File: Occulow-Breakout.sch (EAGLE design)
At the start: 18 parts

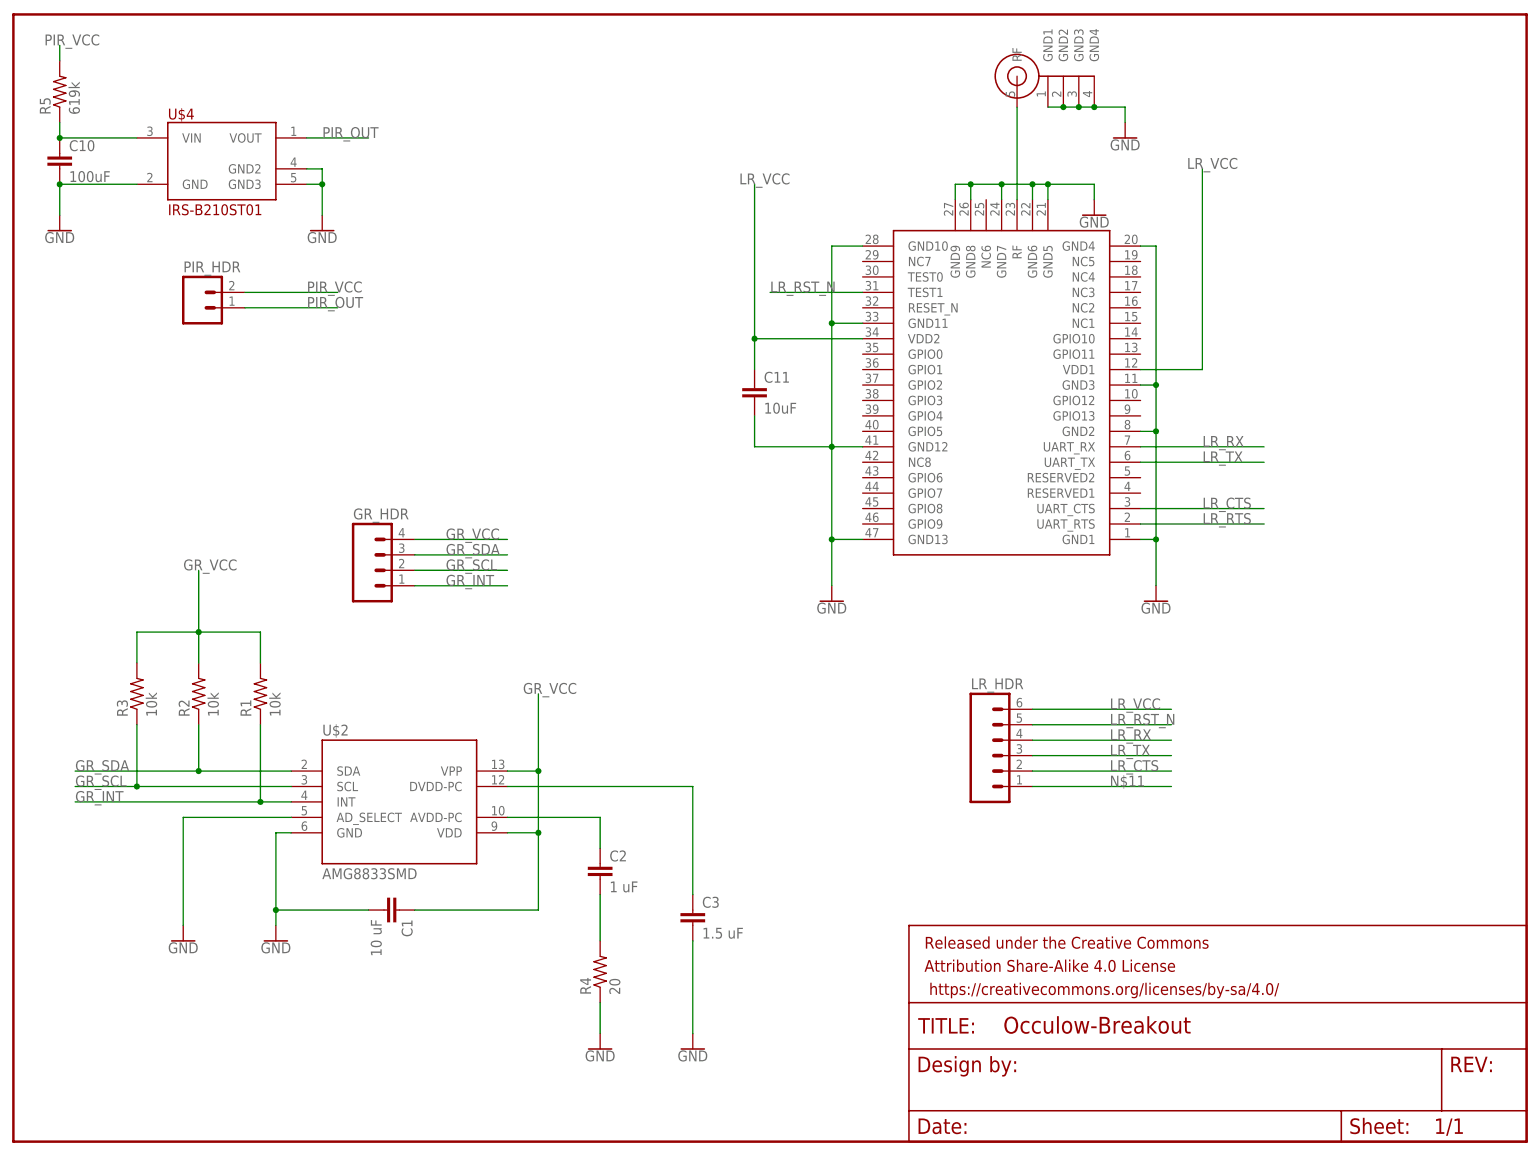
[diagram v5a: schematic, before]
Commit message: Ground pins on headers
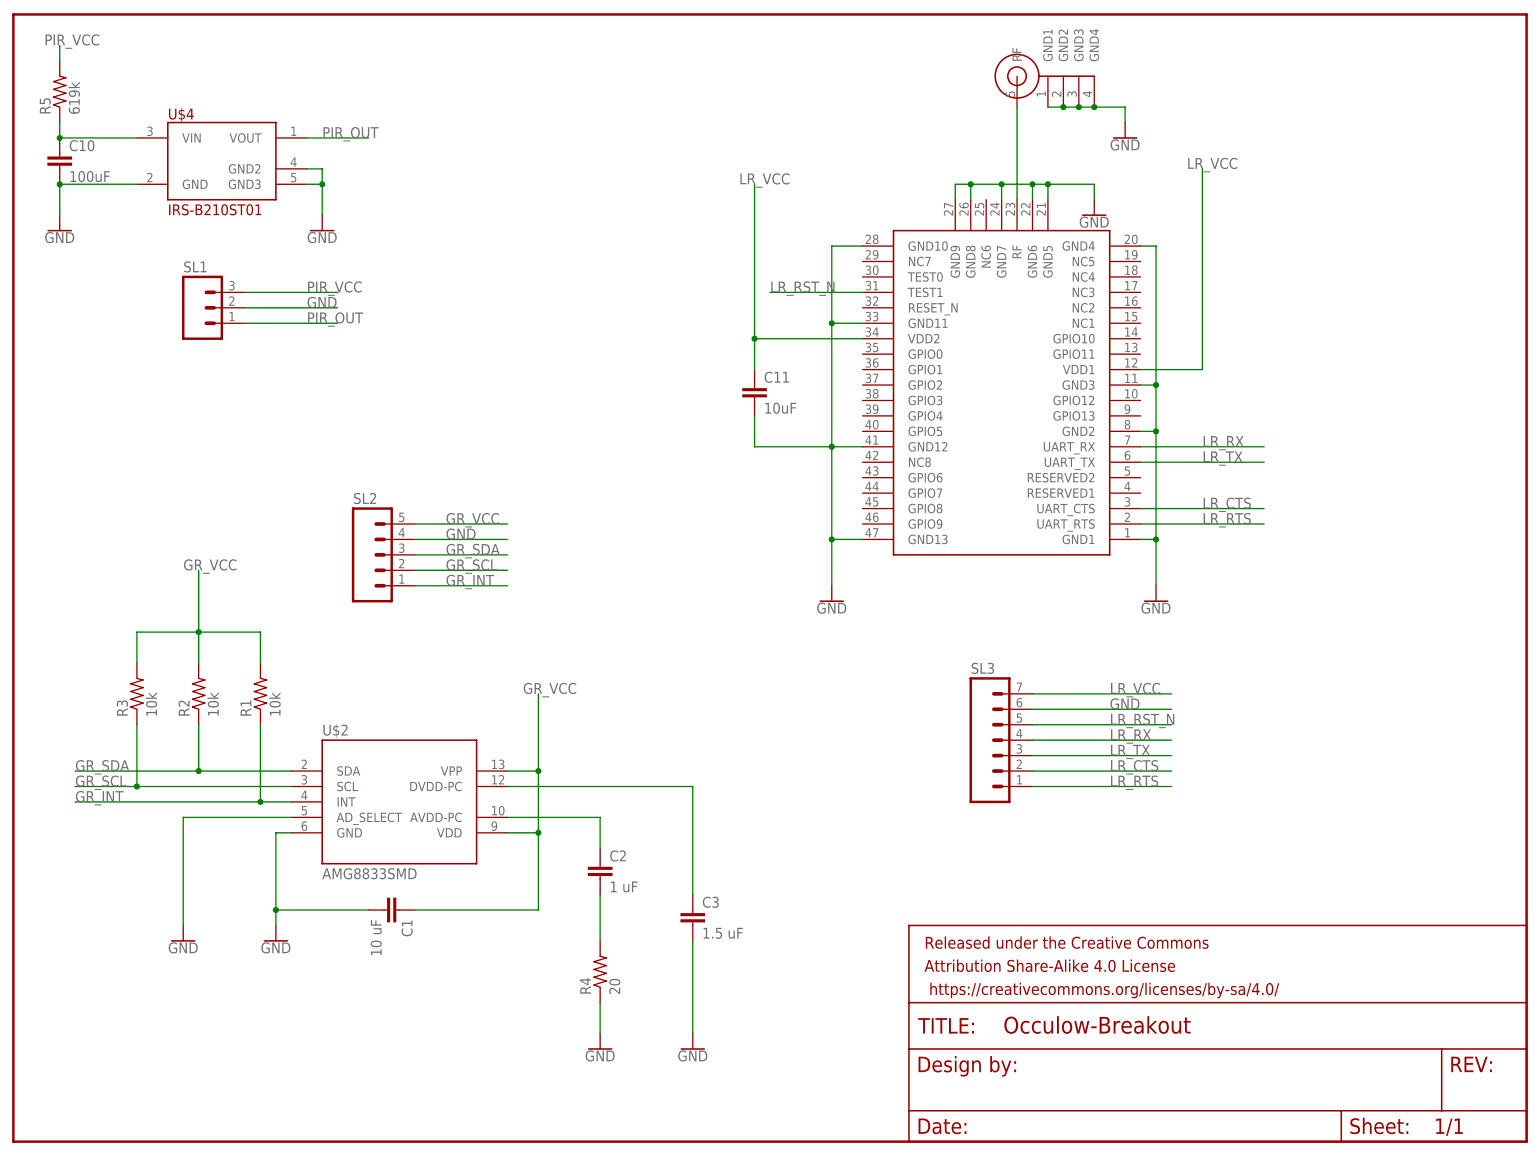
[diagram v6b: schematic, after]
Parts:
- removed GR_HDR: (no value), con-amp-quick:M04
- removed LR_HDR: (no value), con-amp-quick:M06
- removed PIR_HDR: (no value), con-amp-quick:M02
- added SL1: (no value), con-amp-quick:M03
- added SL2: (no value), con-amp-quick:M05
- added SL3: (no value), con-amp-quick:M07
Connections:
- removed net N$11: LR_HDR.1
- net GND: now also SL1.2, SL2.4, SL3.6
- net GR_INT: now also SL2.1; no longer GR_HDR.1
- net GR_SCL: now also SL2.2; no longer GR_HDR.2
- net GR_SDA: now also SL2.3; no longer GR_HDR.3
- net GR_VCC: now also SL2.5; no longer GR_HDR.4
- net LR_CTS: now also SL3.2; no longer LR_HDR.2
- net LR_RST_N: now also SL3.5; no longer LR_HDR.5
- net LR_RTS: now also SL3.1
- net LR_RX: now also SL3.4; no longer LR_HDR.4
- net LR_TX: now also SL3.3; no longer LR_HDR.3
- net LR_VCC: now also SL3.7; no longer LR_HDR.6
- net PIR_OUT: now also SL1.1; no longer PIR_HDR.1
- net PIR_VCC: now also SL1.3; no longer PIR_HDR.2
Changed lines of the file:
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@@
 <part name="R5" library="resistor" deviceset="R-US_" device="R1206" value="619k"/>
 <part name="C11" library="rcl" deviceset="C-EU" device="C1206" value="10uF"/>
-<part name="PIR_HDR" library="con-amp-quick" deviceset="M02" device=""/>
-<part name="GR_HDR" library="con-amp-quick" deviceset="M04" device=""/>
-<part name="LR_HDR" library="con-amp-quick" deviceset="M06" device=""/>
+<part name="SL1" library="con-amp-quick" deviceset="M03" device=""/>
+<part name="SL2" library="con-amp-quick" deviceset="M05" device=""/>
+<part name="SL3" library="con-amp-quick" deviceset="M07" device=""/>
 </parts>
 <sheets>
@@
 <instance part="R5" gate="G$1" x="170.18" y="167.64" rot="R90"/>
 <instance part="C11" gate="G$1" x="284.48" y="119.38"/>
-<instance part="PIR_HDR" gate="G$1" x="193.04" y="132.08"/>
-<instance part="GR_HDR" gate="G$1" x="223.52" y="88.9"/>
-<instance part="LR_HDR" gate="G$1" x="325.12" y="58.42"/>
+<instance part="SL1" gate="G$1" x="193.04" y="132.08"/>
+<instance part="SL2" gate="G$1" x="220.98" y="91.44"/>
+<instance part="SL3" gate="G$1" x="325.12" y="58.42"/>
 </instances>
 <busses>
@@
 </segment>
 <segment>
-<pinref part="GR_HDR" gate="G$1" pin="3"/>
 <wire x1="228.6" y1="91.44" x2="243.84" y2="91.44" width="0.1524" layer="91"/>
 <label x="233.68" y="91.44" size="1.778" layer="95"/>
+<pinref part="SL2" gate="G$1" pin="3"/>
 </segment>
 </net>
@@
 </segment>
 <segment>
-<pinref part="GR_HDR" gate="G$1" pin="2"/>
 <wire x1="228.6" y1="88.9" x2="243.84" y2="88.9" width="0.1524" layer="91"/>
 <label x="233.68" y="88.9" size="1.778" layer="95"/>
+<pinref part="SL2" gate="G$1" pin="2"/>
 </segment>
 </net>
@@
 </segment>
 <segment>
-<pinref part="GR_HDR" gate="G$1" pin="1"/>
 <wire x1="228.6" y1="86.36" x2="243.84" y2="86.36" width="0.1524" layer="91"/>
 <label x="233.68" y="86.36" size="1.778" layer="95"/>
+<pinref part="SL2" gate="G$1" pin="1"/>
 </segment>
 </net>
@@
 <junction x="170.18" y="152.4"/>
 </segment>
+<segment>
+<wire x1="200.66" y1="132.08" x2="215.9" y2="132.08" width="0.1524" layer="91"/>
+<label x="210.82" y="132.08" size="1.778" layer="95"/>
+<pinref part="SL1" gate="G$1" pin="2"/>
+</segment>
+<segment>
+<wire x1="228.6" y1="93.98" x2="243.84" y2="93.98" width="0.1524" layer="91"/>
+<label x="233.68" y="93.98" size="1.778" layer="95"/>
+<pinref part="SL2" gate="G$1" pin="4"/>
+</segment>
+<segment>
+<wire x1="330.2" y1="66.04" x2="353.06" y2="66.04" width="0.1524" layer="91"/>
+<label x="342.9" y="66.04" size="1.778" layer="95"/>
+<pinref part="SL3" gate="G$1" pin="6"/>
+</segment>
 </net>
 <net name="N$2" class="0">
@@
 </segment>
 <segment>
-<pinref part="LR_HDR" gate="G$1" pin="4"/>
 <wire x1="330.2" y1="60.96" x2="353.06" y2="60.96" width="0.1524" layer="91"/>
 <label x="342.9" y="60.96" size="1.778" layer="95"/>
+<pinref part="SL3" gate="G$1" pin="4"/>
 </segment>
 </net>
@@
 </segment>
 <segment>
-<pinref part="LR_HDR" gate="G$1" pin="3"/>
 <wire x1="330.2" y1="58.42" x2="353.06" y2="58.42" width="0.1524" layer="91"/>
 <label x="342.9" y="58.42" size="1.778" layer="95"/>
+<pinref part="SL3" gate="G$1" pin="3"/>
 </segment>
 </net>
@@
 </segment>
 <segment>
-<pinref part="LR_HDR" gate="G$1" pin="2"/>
 <wire x1="330.2" y1="55.88" x2="353.06" y2="55.88" width="0.1524" layer="91"/>
 <label x="342.9" y="55.88" size="1.778" layer="95"/>
+<pinref part="SL3" gate="G$1" pin="2"/>
 </segment>
 </net>
@@
 <wire x1="347.98" y1="96.52" x2="368.3" y2="96.52" width="0.1524" layer="91"/>
 <label x="358.14" y="96.52" size="1.778" layer="95"/>
+</segment>
+<segment>
+<wire x1="330.2" y1="53.34" x2="353.06" y2="53.34" width="0.1524" layer="91"/>
+<label x="342.9" y="53.34" size="1.778" layer="95"/>
+<pinref part="SL3" gate="G$1" pin="1"/>
 </segment>
 </net>
@@
 </segment>
 <segment>
-<pinref part="PIR_HDR" gate="G$1" pin="1"/>
-<wire x1="200.66" y1="132.08" x2="215.9" y2="132.08" width="0.1524" layer="91"/>
-<label x="210.82" y="132.08" size="1.778" layer="95"/>
+<pinref part="SL1" gate="G$1" pin="1"/>
+<wire x1="200.66" y1="129.54" x2="215.9" y2="129.54" width="0.1524" layer="91"/>
+<label x="210.82" y="129.54" size="1.778" layer="95"/>
 </segment>
 </net>
@@
 </segment>
 <segment>
-<pinref part="GR_HDR" gate="G$1" pin="4"/>
-<wire x1="228.6" y1="93.98" x2="243.84" y2="93.98" width="0.1524" layer="91"/>
-<label x="233.68" y="93.98" size="1.778" layer="95"/>
+<pinref part="SL2" gate="G$1" pin="5"/>
+<wire x1="228.6" y1="96.52" x2="243.84" y2="96.52" width="0.1524" layer="91"/>
+<label x="233.68" y="96.52" size="1.778" layer="95"/>
 </segment>
 </net>
@@
 </segment>
 <segment>
-<pinref part="PIR_HDR" gate="G$1" pin="2"/>
 <wire x1="200.66" y1="134.62" x2="215.9" y2="134.62" width="0.1524" layer="91"/>
 <label x="210.82" y="134.62" size="1.778" layer="95"/>
+<pinref part="SL1" gate="G$1" pin="3"/>
 </segment>
 </net>
@@
 </segment>
 <segment>
-<pinref part="LR_HDR" gate="G$1" pin="6"/>
-<wire x1="330.2" y1="66.04" x2="353.06" y2="66.04" width="0.1524" layer="91"/>
-<label x="342.9" y="66.04" size="1.778" layer="95"/>
+<pinref part="SL3" gate="G$1" pin="7"/>
+<wire x1="330.2" y1="68.58" x2="353.06" y2="68.58" width="0.1524" layer="91"/>
+<label x="342.9" y="68.58" size="1.778" layer="95"/>
 </segment>
 </net>
@@
 </segment>
 <segment>
-<pinref part="LR_HDR" gate="G$1" pin="5"/>
 <wire x1="330.2" y1="63.5" x2="353.06" y2="63.5" width="0.1524" layer="91"/>
 <label x="342.9" y="63.5" size="1.778" layer="95"/>
-</segment>
-</net>
-<net name="N$11" class="0">
-<segment>
-<pinref part="LR_HDR" gate="G$1" pin="1"/>
-<wire x1="330.2" y1="53.34" x2="353.06" y2="53.34" width="0.1524" layer="91"/>
-<label x="342.9" y="53.34" size="1.778" layer="95"/>
-</segment>
-</net>
+<pinref part="SL3" gate="G$1" pin="5"/>
+</segment>
+</net>

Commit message: Routing for lora chip
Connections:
- net N$1 renamed RF
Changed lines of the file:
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@@
 </segment>
 </net>
-<net name="N$1" class="0">
+<net name="RF" class="0">
 <segment>
 <pinref part="U$1" gate="G$1" pin="RF"/>

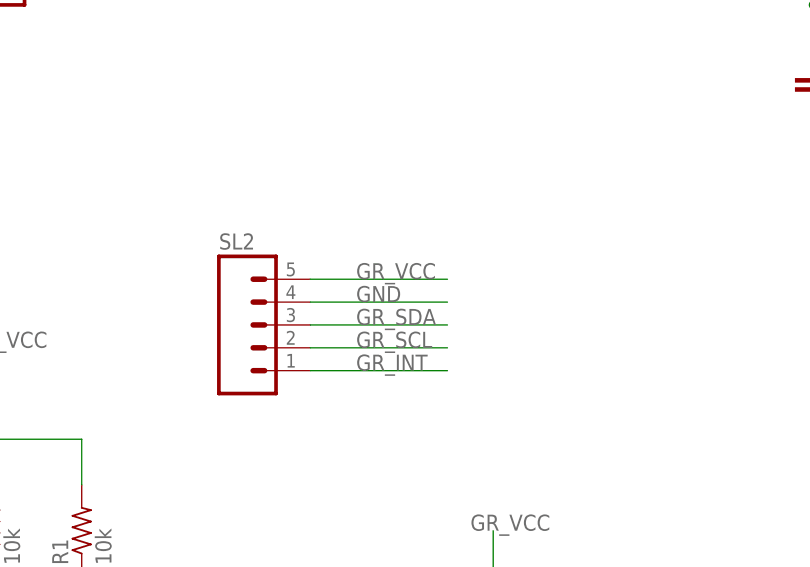
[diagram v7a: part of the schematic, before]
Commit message: Routing for grideye
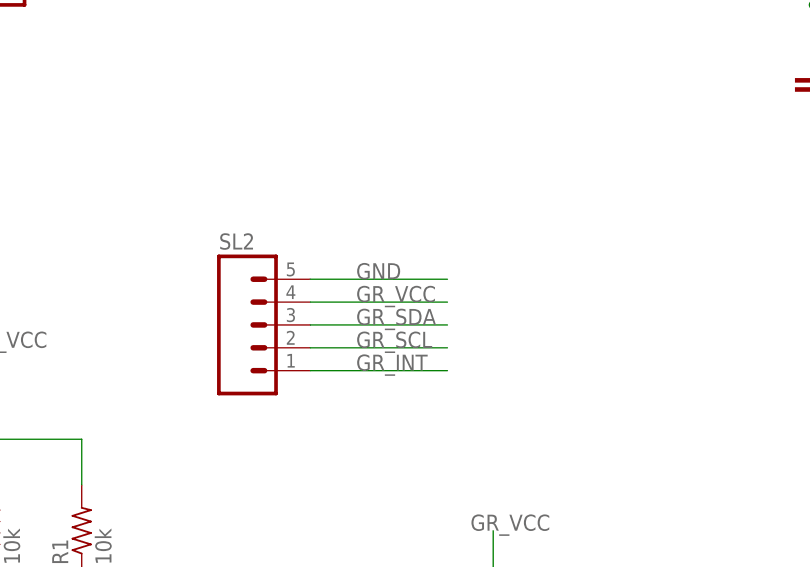
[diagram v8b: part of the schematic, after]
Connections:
- net GND: now also SL2.5; no longer SL2.4
- net GR_VCC: now also SL2.4; no longer SL2.5
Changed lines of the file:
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@@
-</segment>
-<segment>
-<wire x1="228.6" y1="93.98" x2="243.84" y2="93.98" width="0.1524" layer="91"/>
-<label x="233.68" y="93.98" size="1.778" layer="95"/>
-<pinref part="SL2" gate="G$1" pin="4"/>
 </segment>
 <segment>
@@
 <label x="342.9" y="66.04" size="1.778" layer="95"/>
 <pinref part="SL3" gate="G$1" pin="6"/>
+</segment>
+<segment>
+<pinref part="SL2" gate="G$1" pin="5"/>
+<wire x1="228.6" y1="96.52" x2="243.84" y2="96.52" width="0.1524" layer="91"/>
+<label x="233.68" y="96.52" size="1.778" layer="95"/>
 </segment>
 </net>
@@
 </segment>
 <segment>
-<pinref part="SL2" gate="G$1" pin="5"/>
-<wire x1="228.6" y1="96.52" x2="243.84" y2="96.52" width="0.1524" layer="91"/>
-<label x="233.68" y="96.52" size="1.778" layer="95"/>
+<wire x1="228.6" y1="93.98" x2="243.84" y2="93.98" width="0.1524" layer="91"/>
+<label x="233.68" y="93.98" size="1.778" layer="95"/>
+<pinref part="SL2" gate="G$1" pin="4"/>
 </segment>
 </net>
